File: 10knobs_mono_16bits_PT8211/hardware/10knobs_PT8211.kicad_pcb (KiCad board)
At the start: 2 copper layers, 47 parts, among them J1 GND, U1 PT8211, U2 BluePill_STM32F103C, U3 6N138, U4 LM358

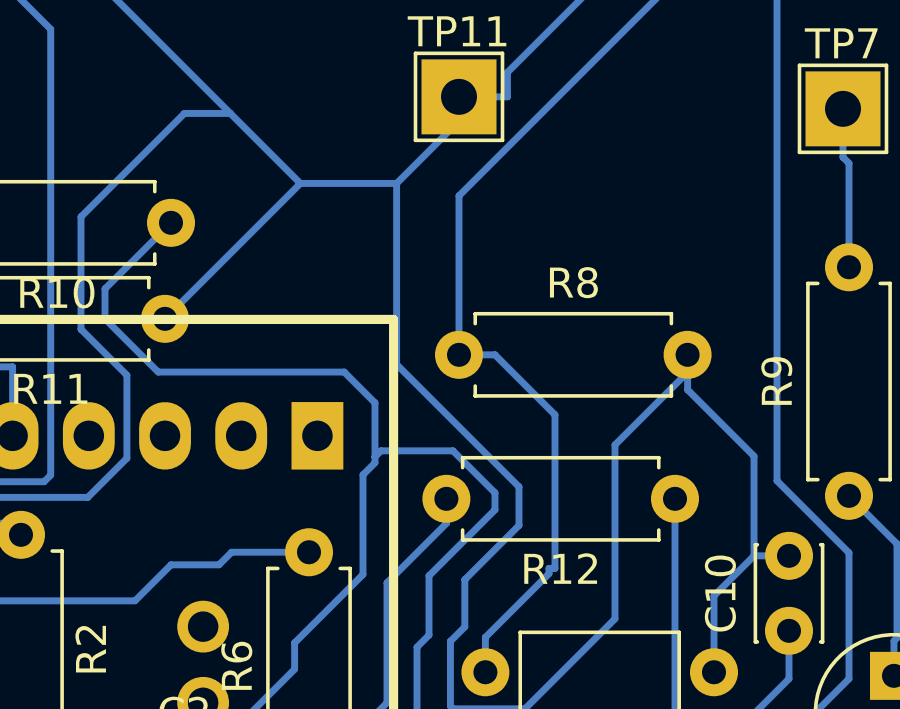
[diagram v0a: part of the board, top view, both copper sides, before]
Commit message: Adjusted lpf
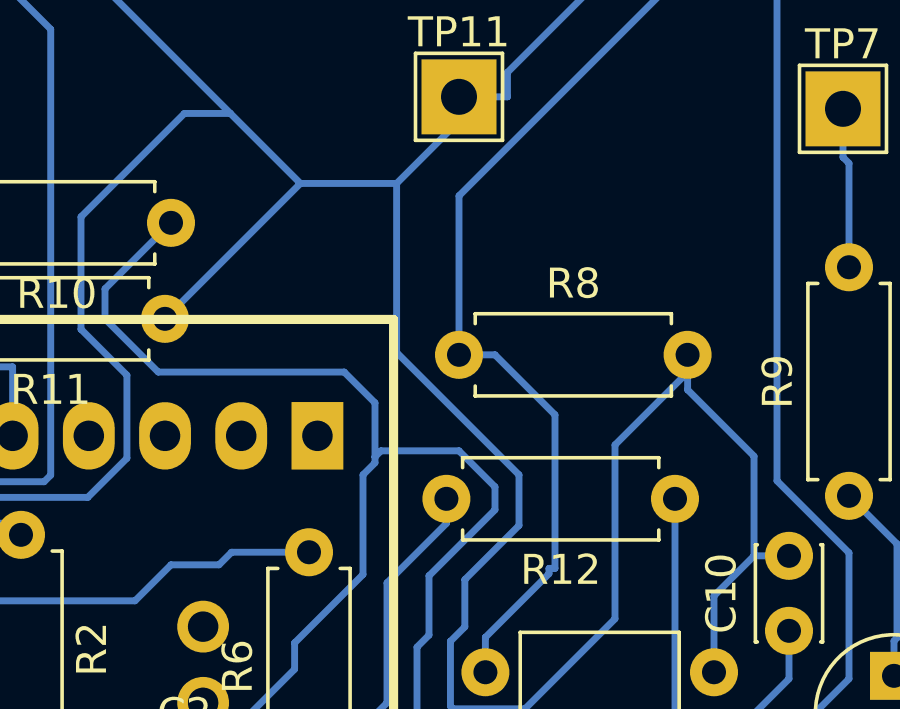
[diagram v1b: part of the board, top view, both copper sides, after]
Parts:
- C10: value 470p -> 680p
- J1: value GND -> Conn_01x06_Female
- R12, R6: value 7.5k -> 10k
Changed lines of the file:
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@@
   (general
     (thickness 1.6)
-    (drawings 14)
+    (drawings 17)
     (tracks 504)
     (zones 0)
@@
       (effects (font (size 1 1) (thickness 0.15)))
     )
-    (fp_text value 7.5k (at 5.2 0.4 90) (layer F.Fab)
+    (fp_text value 10k (at 5.2 0.4 90) (layer F.Fab)
       (effects (font (size 1 1) (thickness 0.15)))
     )
@@
       (effects (font (size 1 1) (thickness 0.15)))
     )
-    (fp_text value GND (at 2.3 0) (layer F.Fab)
+    (fp_text value Conn_01x06_Female (at 2.3 0) (layer F.Fab)
       (effects (font (size 1 1) (thickness 0.15)))
     )
@@
       (effects (font (size 1 1) (thickness 0.15)))
     )
-    (fp_text value 470p (at 1.4 2.8 180) (layer F.Fab)
+    (fp_text value 680p (at 1.4 2.8 180) (layer F.Fab)
       (effects (font (size 1 1) (thickness 0.15)))
     )
@@
       (effects (font (size 1 1) (thickness 0.15)))
     )
-    (fp_text value 7.5k (at 2.6 -0.6 180) (layer F.Fab)
+    (fp_text value 10k (at 2.6 -0.6 180) (layer F.Fab)
       (effects (font (size 1 1) (thickness 0.15)))
     )
@@
     )
   )
+  (gr_line (start 116.8 42.4) (end 123.4 42.4) (layer F.Fab) (width 0.2))
+  (gr_line (start 116.8 42) (end 116.8 42.4) (layer F.Fab) (width 0.2))
+  (gr_line (start 123.4 42) (end 116.8 42) (layer F.Fab) (width 0.2))
   (gr_line (start 101 79) (end 101.8 79) (layer F.Fab) (width 0.2))
   (gr_line (start 101 82.4) (end 101 79) (layer F.Fab) (width 0.2))
@@
   (segment (start 111.6259 75.5516) (end 112.9308 74.2467) (width 0.23) (layer B.Cu) (net 11))
   (segment (start 112.9308 74.2467) (end 112.9308 71.4789) (width 0.23) (layer B.Cu) (net 11))
-  (segment (start 121.9207 71.1207) (end 121.9207 65.087) (width 0.23) (layer B.Cu) (net 11))
-  (segment (start 126 75.2) (end 121.9207 71.1207) (width 0.23) (layer B.Cu) (net 11))
-  (segment (start 126 76.4873) (end 126 75.2) (width 0.23) (layer B.Cu) (net 11))
-  (segment (start 131.62 71.3826) (end 129.2 73.8026) (width 0.23) (layer B.Cu) (net 11))
-  (segment (start 129.2 73.8026) (end 129.2 79.6) (width 0.23) (layer B.Cu) (net 11))
-  (segment (start 126.2 82.6) (end 123.8 82.6) (width 0.23) (layer B.Cu) (net 11))
-  (segment (start 123.8 82.6) (end 123.7146 82.5146) (width 0.23) (layer B.Cu) (net 11))
-  (segment (start 123.7146 82.5146) (end 123.7146 80.348) (width 0.23) (layer B.Cu) (net 11))
-  (segment (start 129.2 79.6) (end 126.2 82.6) (width 0.23) (layer B.Cu) (net 11))
-  (segment (start 123.7146 80.348) (end 124.195 79.8676) (width 0.23) (layer B.Cu) (net 11))
-  (segment (start 124.195 79.8676) (end 124.195 78.2923) (width 0.23) (layer B.Cu) (net 11))
-  (segment (start 124.195 78.2923) (end 126 76.4873) (width 0.23) (layer B.Cu) (net 11))
   (segment (start 90.0298 75.0365) (end 90.0298 68.6298) (width 0.23) (layer B.Cu) (net 11))
   (segment (start 73.4 57) (end 73 57) (width 0.23) (layer B.Cu) (net 11))
@@
   (segment (start 98.1153 93.4) (end 92.65 93.4) (width 0.23) (layer B.Cu) (net 11))
   (segment (start 92.65 93.4) (end 92.65 96.55) (width 0.23) (layer B.Cu) (net 11))
+  (segment (start 126 74.8) (end 121.9207 70.7207) (width 0.23) (layer B.Cu) (net 11))
+  (segment (start 126.2 82.6) (end 123.8 82.6) (width 0.23) (layer B.Cu) (net 11))
+  (segment (start 129.2 79.6) (end 126.2 82.6) (width 0.23) (layer B.Cu) (net 11))
+  (segment (start 129.2 73.8026) (end 129.2 79.6) (width 0.23) (layer B.Cu) (net 11))
+  (segment (start 124.195 79.8676) (end 124.195 78.2923) (width 0.23) (layer B.Cu) (net 11))
+  (segment (start 123.8 82.6) (end 123.7146 82.5146) (width 0.23) (layer B.Cu) (net 11))
+  (segment (start 121.9207 70.7207) (end 121.9207 65.087) (width 0.23) (layer B.Cu) (net 11))
+  (segment (start 126 76.4873) (end 126 74.8) (width 0.23) (layer B.Cu) (net 11))
+  (segment (start 123.7146 82.5146) (end 123.7146 80.348) (width 0.23) (layer B.Cu) (net 11))
+  (segment (start 123.7146 80.348) (end 124.195 79.8676) (width 0.23) (layer B.Cu) (net 11))
+  (segment (start 131.62 71.3826) (end 129.2 73.8026) (width 0.23) (layer B.Cu) (net 11))
+  (segment (start 124.195 78.2923) (end 126 76.4873) (width 0.23) (layer B.Cu) (net 11))
   (segment (start 78.9208 91) (end 81.1808 88.74) (width 0.23) (layer B.Cu) (net 12))
   (segment (start 77.6 91) (end 78.9208 91) (width 0.23) (layer B.Cu) (net 12))
@@
   (segment (start 121.2 72.4) (end 120.1739 71.3739) (width 0.23) (layer B.Cu) (net 34))
   (segment (start 121.2 74.2) (end 121.2 72.4) (width 0.23) (layer B.Cu) (net 34))
-  (segment (start 121.4 74) (end 121.2 74.2) (width 0.23) (layer B.Cu) (net 34))
-  (segment (start 122.6 80.5431) (end 123 80.1431) (width 0.23) (layer B.Cu) (net 34))
   (segment (start 113.9739 71.3739) (end 112.2 69.6) (width 0.23) (layer B.Cu) (net 34))
-  (segment (start 123.7146 84.5146) (end 122.6 83.4) (width 0.23) (layer B.Cu) (net 34))
-  (segment (start 123 78.165) (end 125.2 75.965) (width 0.23) (layer B.Cu) (net 34))
-  (segment (start 122.6 83.4) (end 122.6 80.5431) (width 0.23) (layer B.Cu) (net 34))
-  (segment (start 123.7146 87.8346) (end 123.7146 84.5146) (width 0.23) (layer B.Cu) (net 34))
-  (segment (start 124.88 89) (end 123.7146 87.8346) (width 0.23) (layer B.Cu) (net 34))
-  (segment (start 123 80.1431) (end 123 78.165) (width 0.23) (layer B.Cu) (net 34))
-  (segment (start 123.8 74) (end 121.4 74) (width 0.23) (layer B.Cu) (net 34))
-  (segment (start 125.2 75.965) (end 125.2 75.4) (width 0.23) (layer B.Cu) (net 34))
-  (segment (start 125.2 75.4) (end 123.8 74) (width 0.23) (layer B.Cu) (net 34))
   (segment (start 120.8 74.8) (end 121.2 74.4) (width 0.23) (layer B.Cu) (net 34))
   (segment (start 120.8 78.121162) (end 120.8 74.8) (width 0.23) (layer B.Cu) (net 34))
@@
   (segment (start 117.55 85.75) (end 117.55 84.35) (width 0.23) (layer B.Cu) (net 34))
   (segment (start 121.2 74.2) (end 121.2 74.4) (width 0.23) (layer B.Cu) (net 34))
+  (segment (start 122.6 83.4) (end 122.6 80.5431) (width 0.23) (layer B.Cu) (net 34))
+  (segment (start 123.7146 84.5146) (end 122.6 83.4) (width 0.23) (layer B.Cu) (net 34))
+  (segment (start 124.88 89) (end 123.7146 87.8346) (width 0.23) (layer B.Cu) (net 34))
+  (segment (start 124 74) (end 121.4 74) (width 0.23) (layer B.Cu) (net 34))
+  (segment (start 125.2 75.965) (end 125.2 75.2) (width 0.23) (layer B.Cu) (net 34))
+  (segment (start 122.6 80.5431) (end 123 80.1431) (width 0.23) (layer B.Cu) (net 34))
+  (segment (start 123 80.1431) (end 123 78.165) (width 0.23) (layer B.Cu) (net 34))
+  (segment (start 123 78.165) (end 125.2 75.965) (width 0.23) (layer B.Cu) (net 34))
+  (segment (start 121.4 74) (end 121.2 74.2) (width 0.23) (layer B.Cu) (net 34))
+  (segment (start 123.7146 87.8346) (end 123.7146 84.5146) (width 0.23) (layer B.Cu) (net 34))
+  (segment (start 125.2 75.2) (end 124 74) (width 0.23) (layer B.Cu) (net 34))
   (segment (start 114.4 77.8) (end 116 77.8) (width 0.23) (layer B.Cu) (net 35))
   (segment (start 116.42 77.38) (end 119 77.38) (width 0.23) (layer B.Cu) (net 35))
